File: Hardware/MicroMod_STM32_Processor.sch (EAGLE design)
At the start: 37 parts, among them J1 MICROMOD-2222, Q1 MOSFET_PCH-DMG2305UX-7, U1 STM32F405RGT6, U3 W25QXX128MBIT-6X5, Y1 12MHz, Y2 32.768kHz

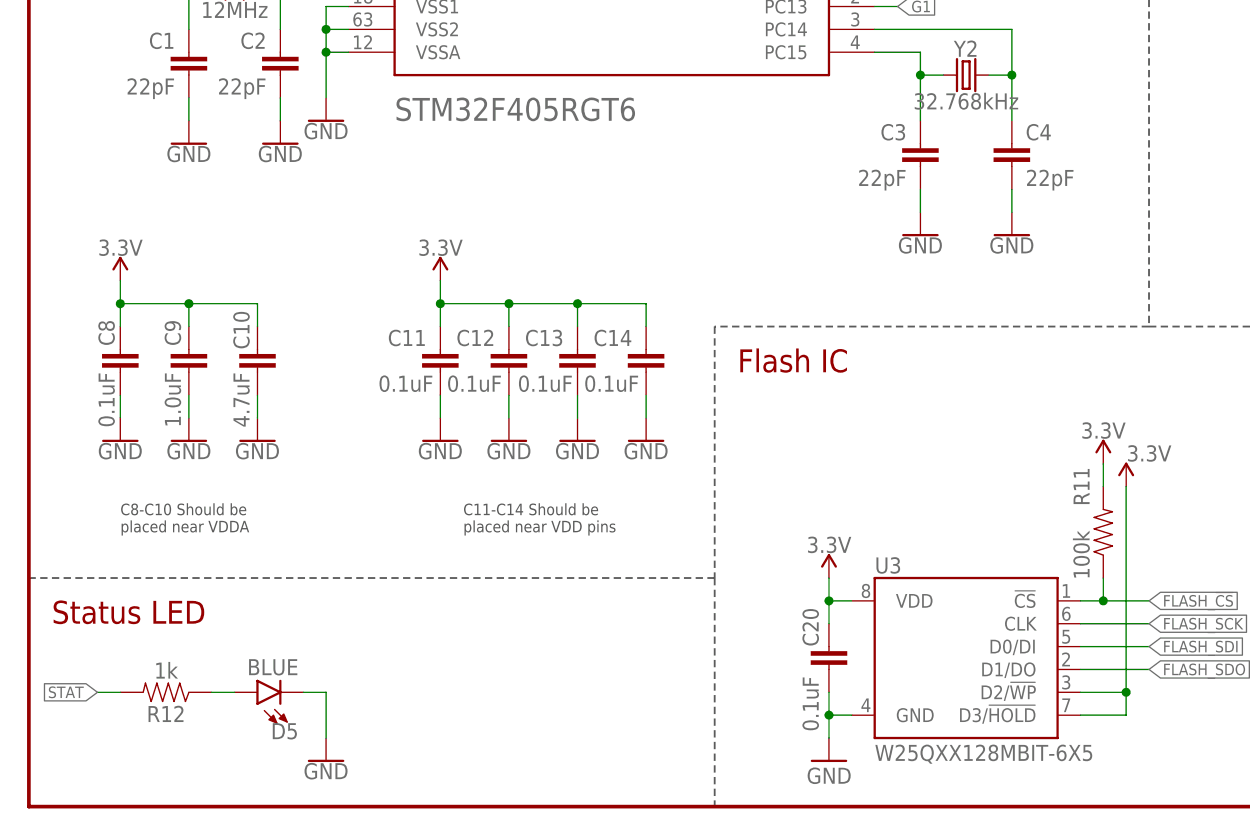
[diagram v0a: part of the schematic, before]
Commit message: V01 Update
Added jumper for USB host config
Updated crystal caps
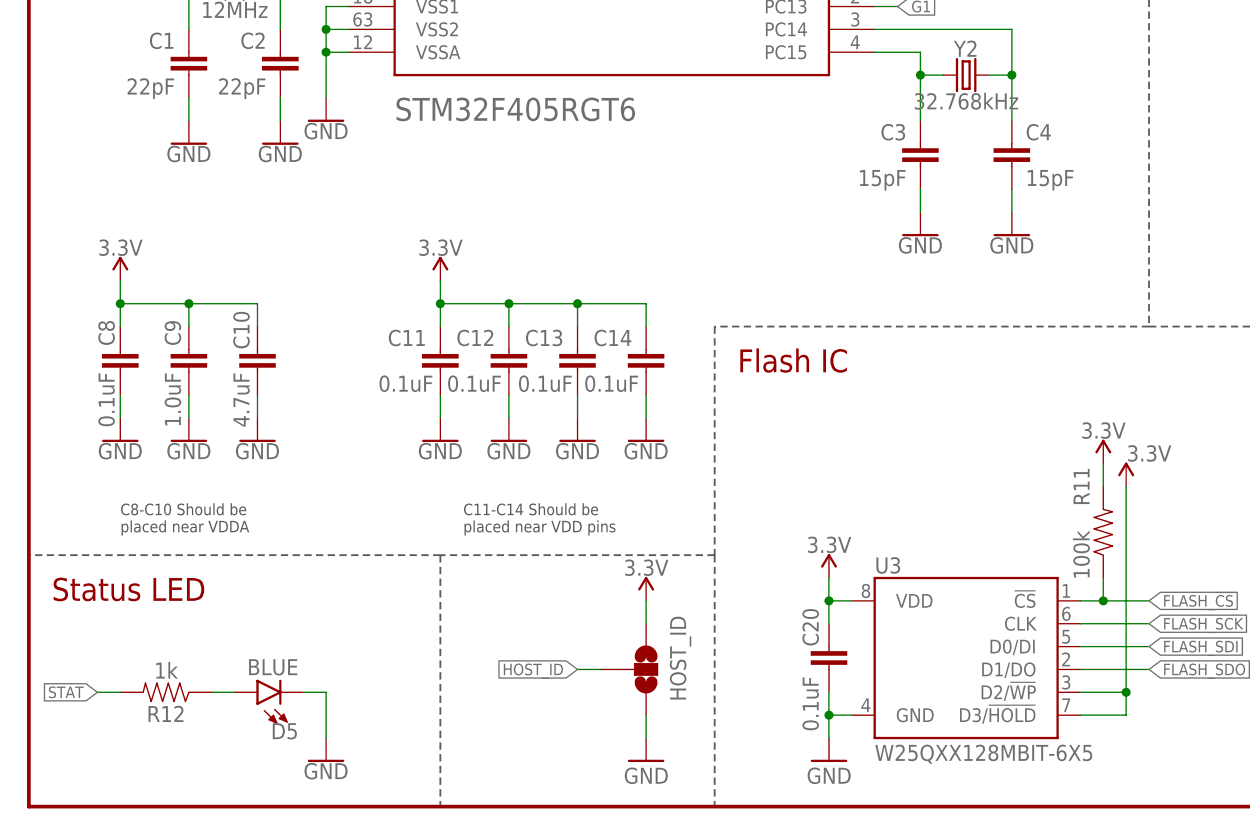
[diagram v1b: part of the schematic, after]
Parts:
- added HOST_ID: JUMPER-SMT_3_NO_NO-SILK, SparkFun-Jumpers:JUMPER-SMT_3_NO_NO-SILK
- C3, C4: value 22pF -> 15pF; device SparkFun-Capacitors:22PF-0402T-16V-10% -> SparkFun-Capacitors:15PF-0402T-50V-5%
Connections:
- net 3.3V: now also HOST_ID.1
- net GND: now also HOST_ID.3
- net HOST_ID: now also HOST_ID.2

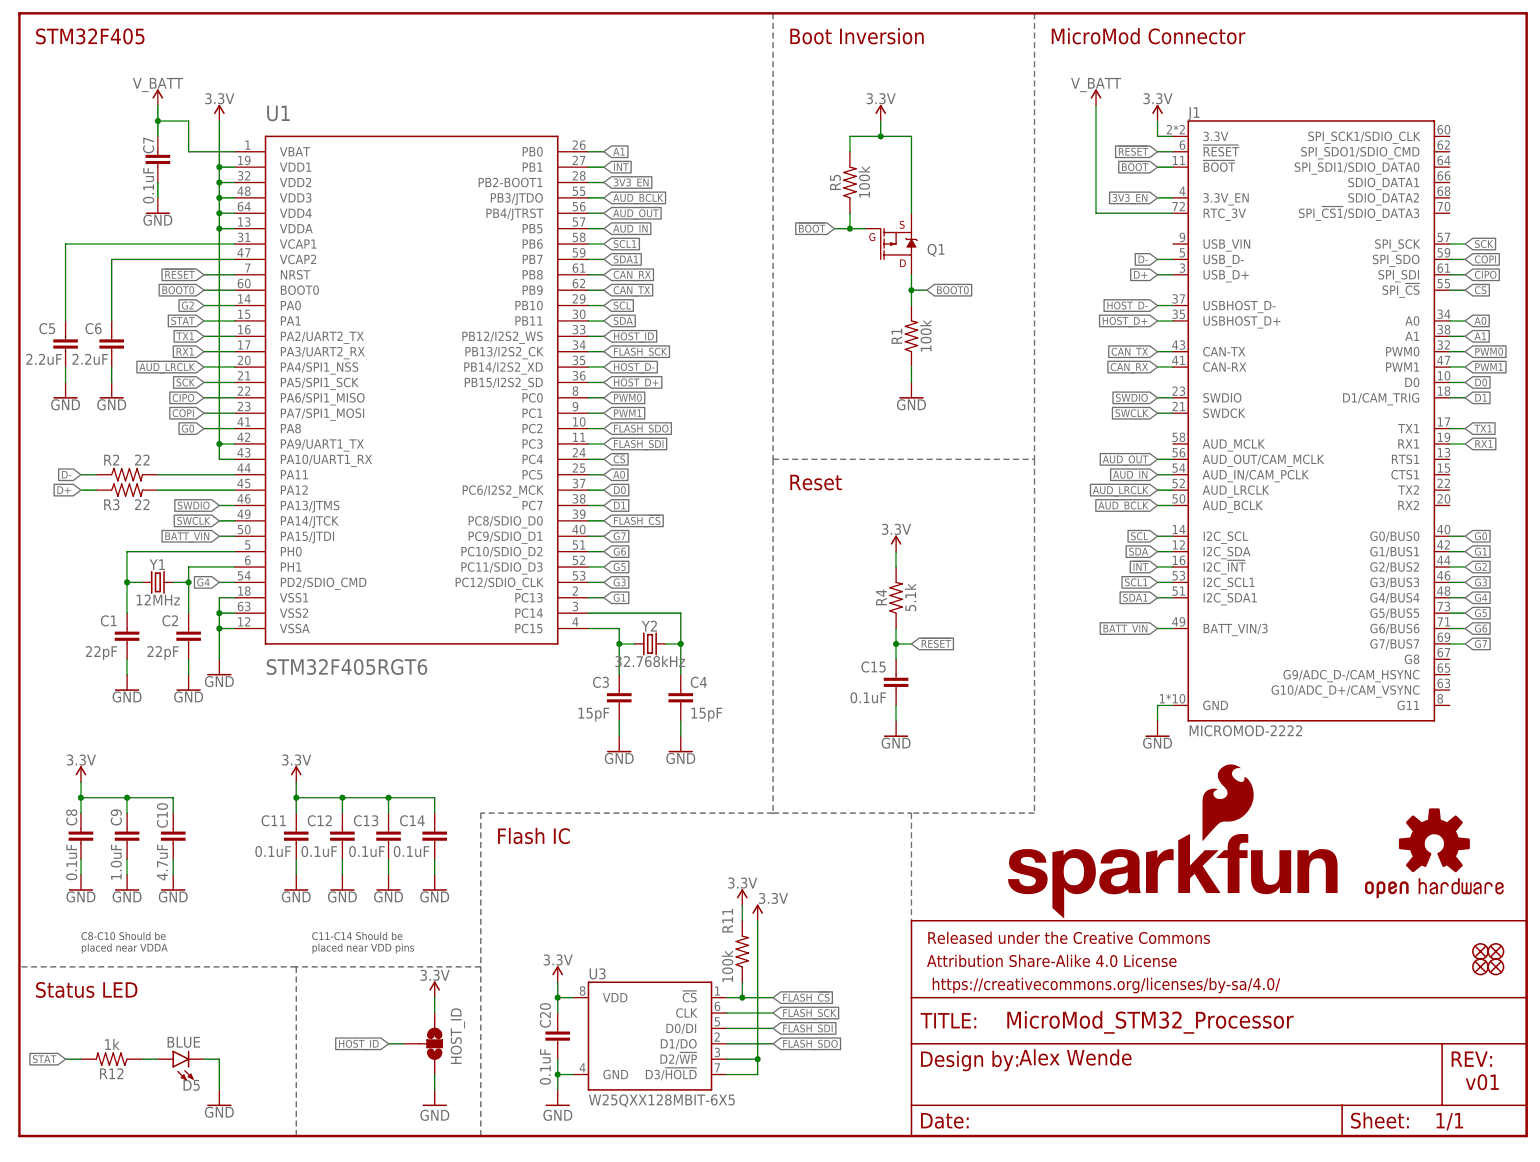
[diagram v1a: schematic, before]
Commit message: The 'ol pin switch-a-roo
- Swapped D0/D1 with PWM0/1 - PWM pins weren't capable of PWM
- Swapped BATT_VIN with STAT - BATT_VIN needs to be on an ADC pin
- Moved PB13 to G10 - Based on testing VBUS needs to be broken out or pulled high for USB HS/FS to work correctly
- Moved PB12 from jumper to G11 for USB Host ID to match with SAMD51 MM
- Reorganized G0-G6 for better routing
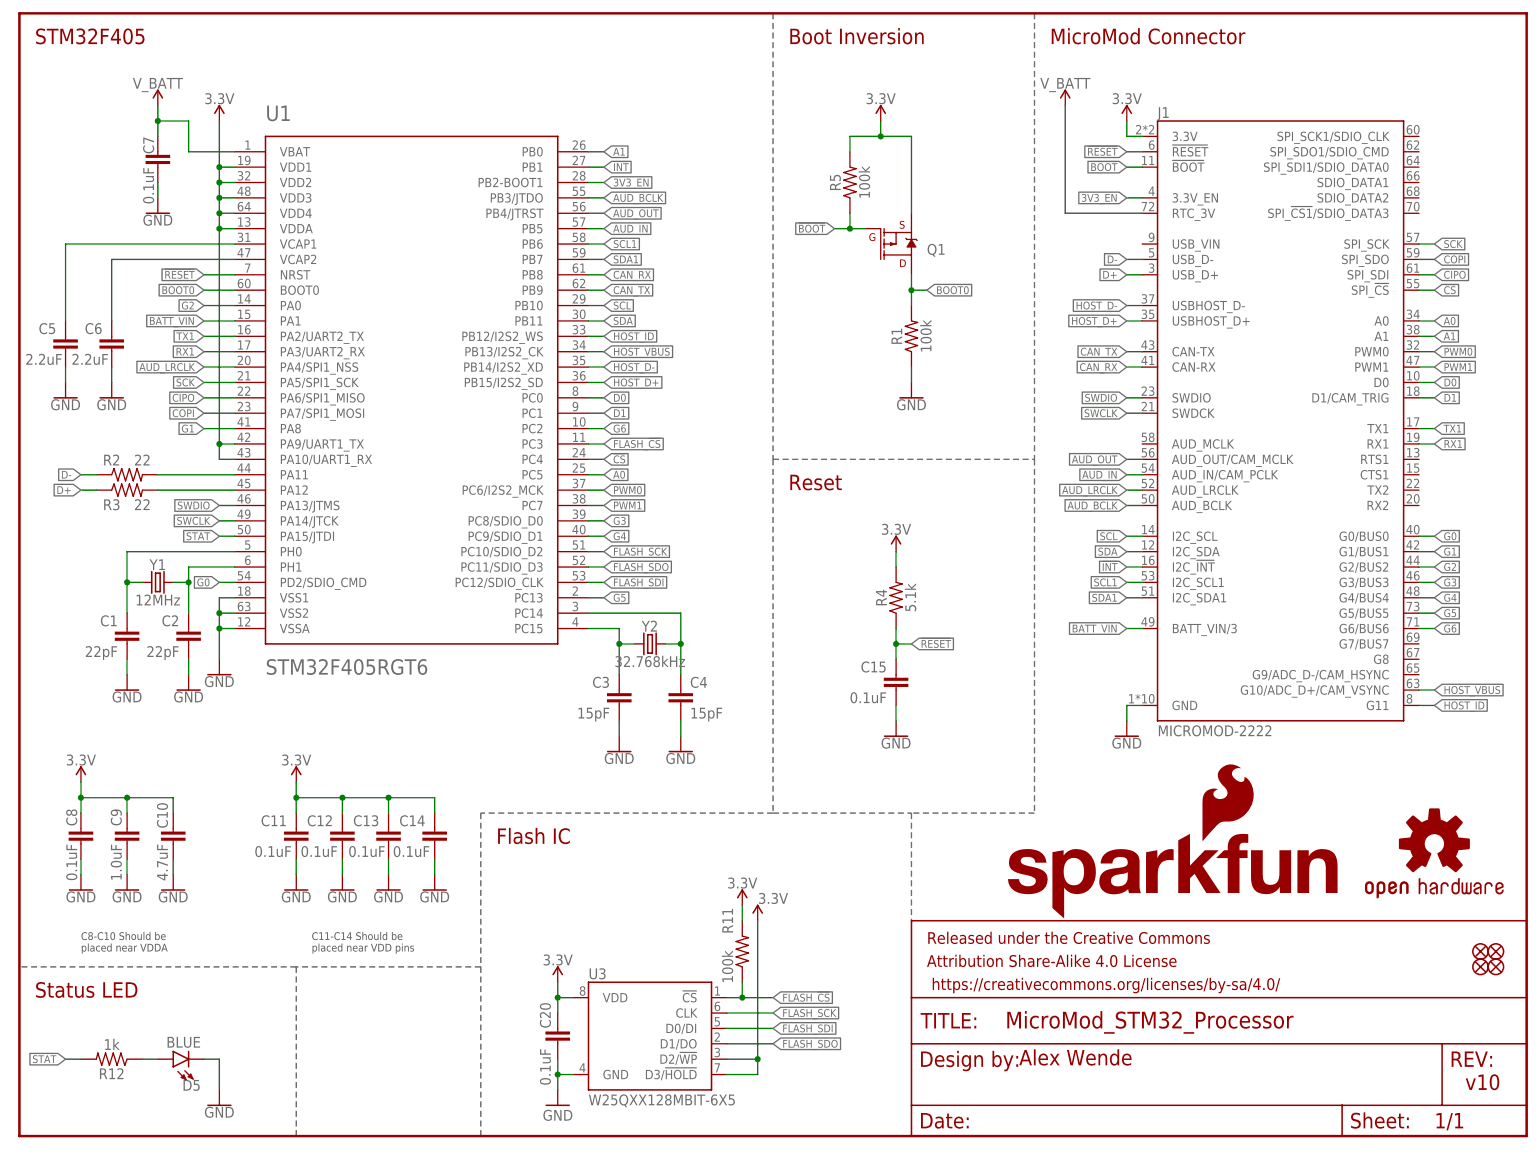
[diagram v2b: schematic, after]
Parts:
- removed HOST_ID: JUMPER-SMT_3_NO_NO-SILK, SparkFun-Jumpers:JUMPER-SMT_3_NO_NO-SILK
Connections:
- removed net G7: J1.G7/BUS7, U1.PC9/SDIO_D1
- new net HOST_VBUS: J1.G10/ADC_D+/CAM_VSYNC, U1.PB13/I2S2_CK
- net 3.3V: no longer HOST_ID.1
- net BATT_VIN: now also U1.PA1; no longer U1.PA15/JTDI
- net D0: now also U1.PC0; no longer U1.PC6/I2S2_MCK
- net D1: now also U1.PC1; no longer U1.PC7
- net FLASH_!CS: now also U1.PC3; no longer U1.PC8/SDIO_D0
- net FLASH_SCK: now also U1.PC10/SDIO_D2; no longer U1.PB13/I2S2_CK
- net FLASH_SDI: now also U1.PC12/SDIO_CLK; no longer U1.PC3
- net FLASH_SDO: now also U1.PC11/SDIO_D3; no longer U1.PC2
- net G0: now also U1.PD2/SDIO_CMD; no longer U1.PA8
- net G1: now also U1.PA8; no longer U1.PC13
- net G3: now also U1.PC8/SDIO_D0; no longer U1.PC12/SDIO_CLK
- net G4: now also U1.PC9/SDIO_D1; no longer U1.PD2/SDIO_CMD
- net G5: now also U1.PC13; no longer U1.PC11/SDIO_D3
- net G6: now also U1.PC2; no longer U1.PC10/SDIO_D2
- net GND: no longer HOST_ID.3
- net HOST_ID: now also J1.G11; no longer HOST_ID.2
- net PWM0: now also U1.PC6/I2S2_MCK; no longer U1.PC0
- net PWM1: now also U1.PC7; no longer U1.PC1
- net STAT: now also U1.PA15/JTDI; no longer U1.PA1
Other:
- note added: "v10"
- note removed: "v01"
- moved on the sheet: J1
